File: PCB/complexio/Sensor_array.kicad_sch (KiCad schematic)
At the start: 69 parts, among them J1 Conn_01x21_Pin, Q1 AO3400A, U10 KTIR0711S, U11 KTIR0711S, U12 KTIR0711S, U13 KTIR0711S, U14 KTIR0711S, U15 KTIR0711S, U16 KTIR0711S, U17 KTIR0711S, U18 KTIR0711S, U19 KTIR0711S, U20 SN74LVC16T245DGGR, U4 KTIR0711S, U5 KTIR0711S, U6 KTIR0711S, U7 KTIR0711S, U8 KTIR0711S, U9 KTIR0711S

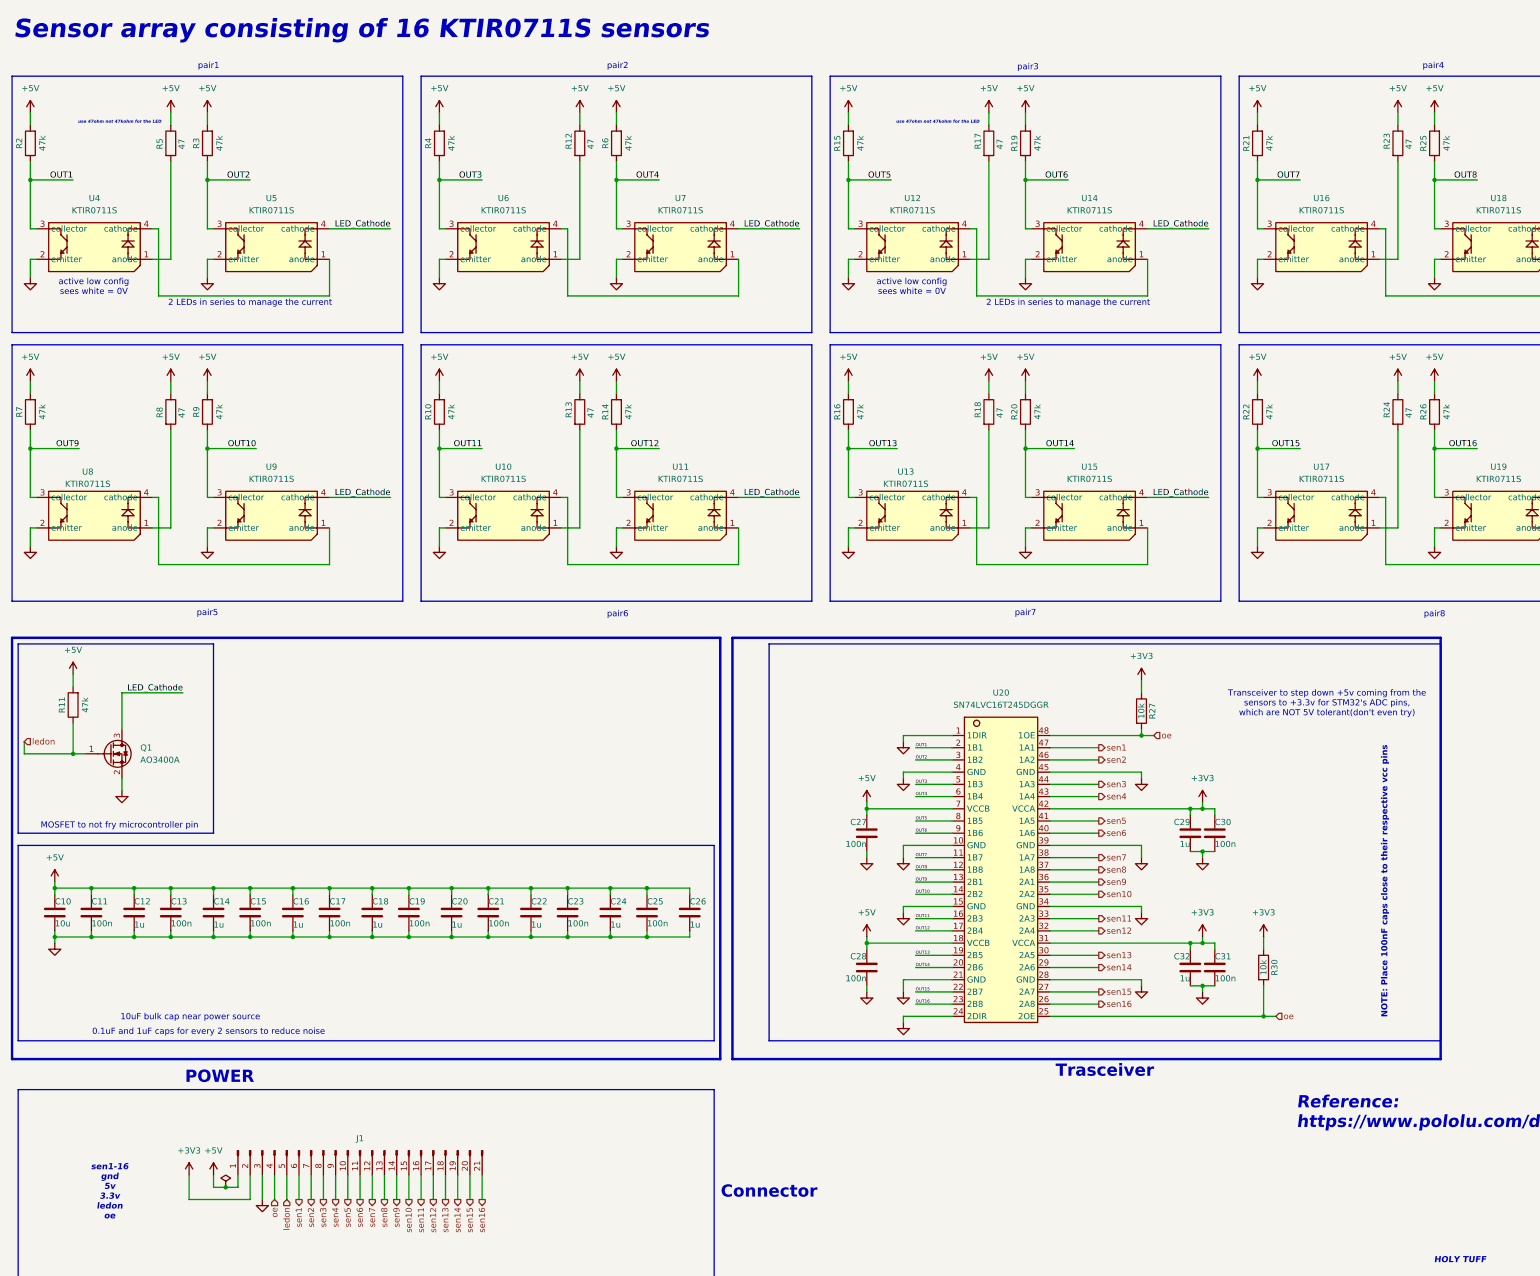
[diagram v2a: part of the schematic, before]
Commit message: Advanced with schem & resolved main power problem
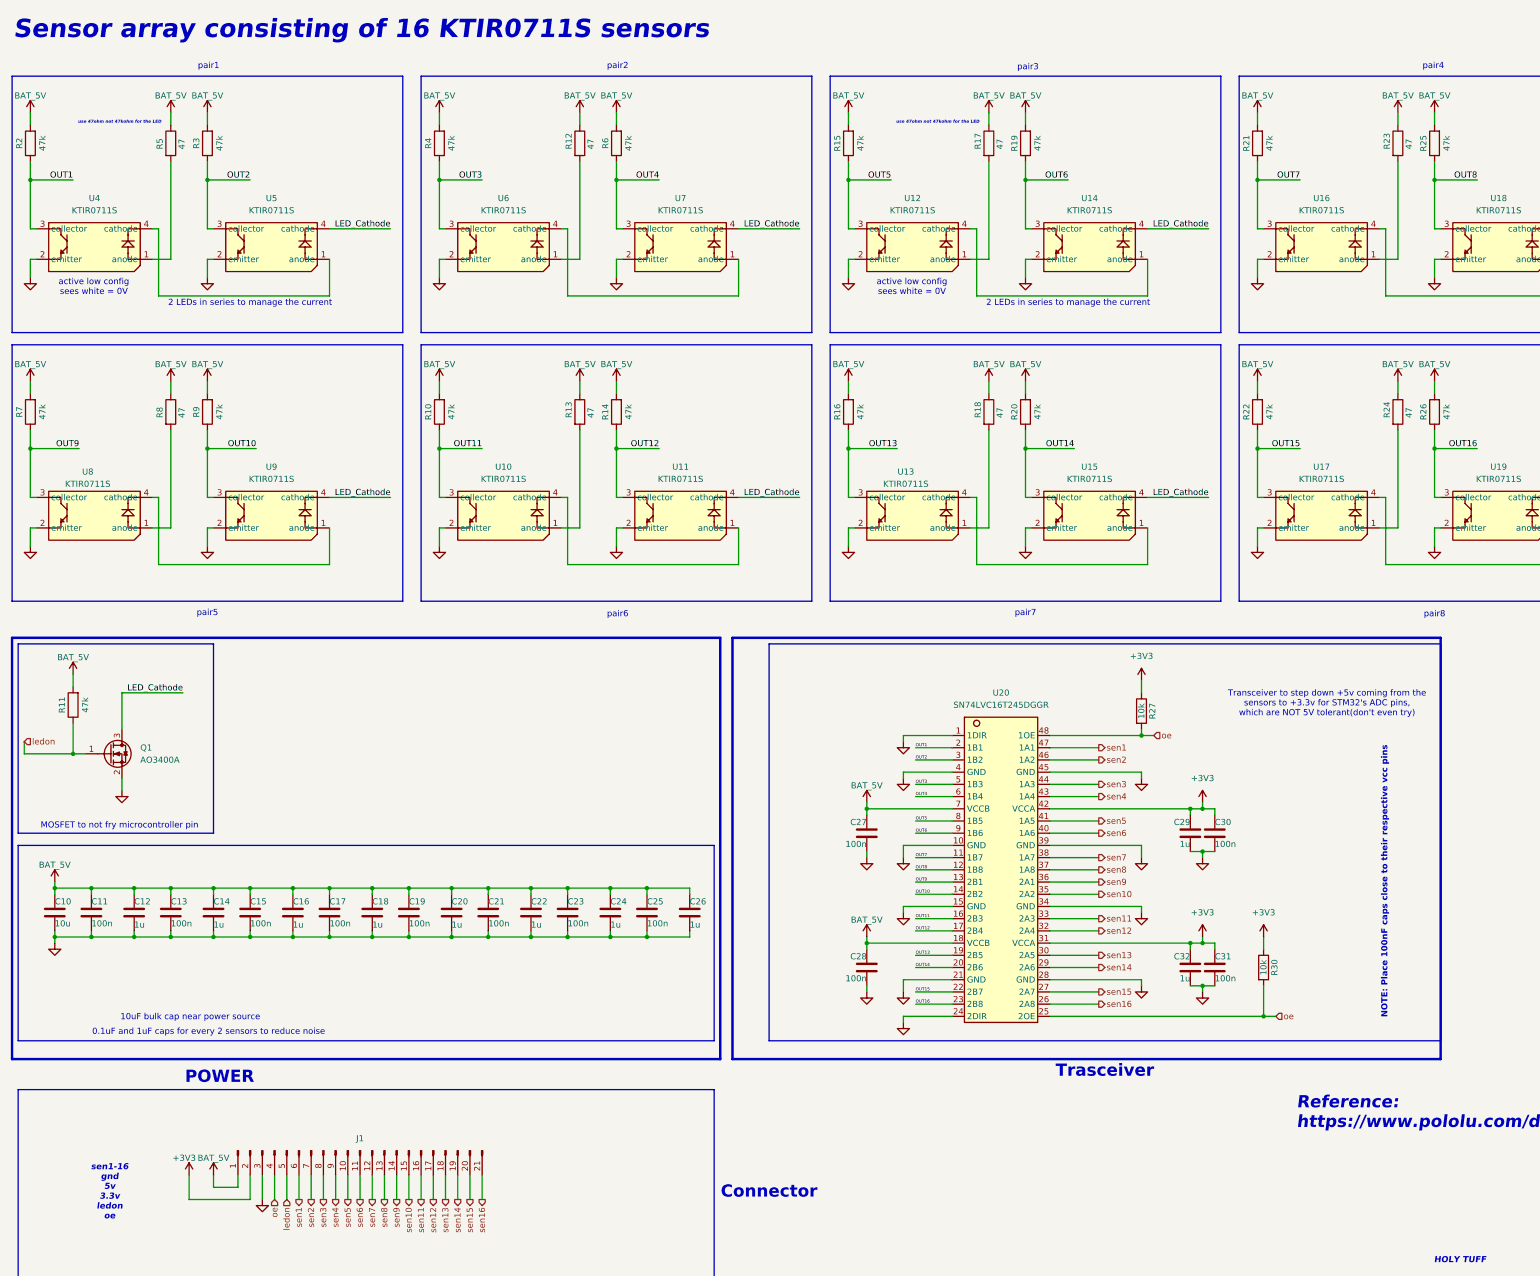
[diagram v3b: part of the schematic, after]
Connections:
- net +5V renamed BAT_5V
